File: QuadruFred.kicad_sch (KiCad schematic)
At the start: 0 parts

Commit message: Add basic leg boards and eps 32. No in depth wiring done.
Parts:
- added J1: Servo1, Connector_PinHeader_2.54mm:PinHeader_1x03_P2.54mm_Horizontal, symbol Connector:Conn_01x03_Pin
- added J10: Servo10, Connector_PinHeader_2.54mm:PinHeader_1x03_P2.54mm_Horizontal, symbol Connector:Conn_01x03_Pin
- added J11: Servo11, Connector_PinHeader_2.54mm:PinHeader_1x03_P2.54mm_Horizontal, symbol Connector:Conn_01x03_Pin
- added J12: Servo12, Connector_PinHeader_2.54mm:PinHeader_1x03_P2.54mm_Horizontal, symbol Connector:Conn_01x03_Pin
- added J2: Servo2, Connector_PinHeader_2.54mm:PinHeader_1x03_P2.54mm_Horizontal, symbol Connector:Conn_01x03_Pin
- added J3: Servo 3, Connector_PinHeader_2.54mm:PinHeader_1x03_P2.54mm_Horizontal, symbol Connector:Conn_01x03_Pin
- added J4: Servo4, Connector_PinHeader_2.54mm:PinHeader_1x03_P2.54mm_Horizontal, symbol Connector:Conn_01x03_Pin
- added J5: Servo5, Connector_PinHeader_2.54mm:PinHeader_1x03_P2.54mm_Horizontal, symbol Connector:Conn_01x03_Pin
- added J6: Servo6, Connector_PinHeader_2.54mm:PinHeader_1x03_P2.54mm_Horizontal, symbol Connector:Conn_01x03_Pin
- added J7: Servo7, Connector_PinHeader_2.54mm:PinHeader_1x03_P2.54mm_Horizontal, symbol Connector:Conn_01x03_Pin
- added J8: Servo8, Connector_PinHeader_2.54mm:PinHeader_1x03_P2.54mm_Horizontal, symbol Connector:Conn_01x03_Pin
- added J9: Servo9, Connector_PinHeader_2.54mm:PinHeader_1x03_P2.54mm_Horizontal, symbol Connector:Conn_01x03_Pin
- added U1: PCA9685PW, Package_SO:TSSOP-28_4.4x9.7mm_P0.65mm, symbol Driver_LED:PCA9685PW
- added U2: ESP32-S3-MINI-1, RF_Module:ESP32-S2-MINI-1, symbol RF_Module:ESP32-S3-MINI-1
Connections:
- new net: J7.1 (Pin_1), U1.12 (LED6)
- new net: U2.1 (GND), U2.2 (GND), U2.42 (GND), U2.43 (GND), U2.46 (GND), U2.47 (GND), U2.48 (GND), U2.49 (GND), U2.50 (GND), U2.51 (GND), U2.52 (GND), U2.53 (GND), U2.54 (GND), U2.55 (GND), U2.56 (GND), U2.57 (GND), U2.58 (GND), U2.59 (GND), U2.60 (GND), U2.61 (GND), U2.62 (GND), U2.63 (GND), U2.64 (GND), U2.65 (GND)
- new net: J8.1 (Pin_1), U1.13 (LED7)
- new net: J10.1 (Pin_1), U1.16 (LED9)
- new net: J1.1 (Pin_1), U1.6 (LED0)
- new net: J5.1 (Pin_1), U1.10 (LED4)
- new net: J6.1 (Pin_1), U1.11 (LED5)
- new net: J9.1 (Pin_1), U1.15 (LED8)
- new net: J11.1 (Pin_1), U1.17 (LED10)
- new net: J12.1 (Pin_1), U1.18 (LED11)
- new net: J2.1 (Pin_1), U1.7 (LED1)
- new net: J3.1 (Pin_1), U1.8 (LED2)
- new net: J4.1 (Pin_1), U1.9 (LED3)
- new net +5V: J1.2 (Pin_2), J10.2 (Pin_2), J11.2 (Pin_2), J12.2 (Pin_2), J2.2 (Pin_2), J3.2 (Pin_2), J4.2 (Pin_2), J5.2 (Pin_2), J6.2 (Pin_2), J7.2 (Pin_2), J8.2 (Pin_2), J9.2 (Pin_2), U1.28 (VDD)
- new net GND: J1.3 (Pin_3), J10.3 (Pin_3), J11.3 (Pin_3), J12.3 (Pin_3), J2.3 (Pin_3), J3.3 (Pin_3), J4.3 (Pin_3), J5.3 (Pin_3), J6.3 (Pin_3), J7.3 (Pin_3), J8.3 (Pin_3), J9.3 (Pin_3), U1.14 (VSS)
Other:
- note added: "Leg PWM System"
- note added: "Legs"

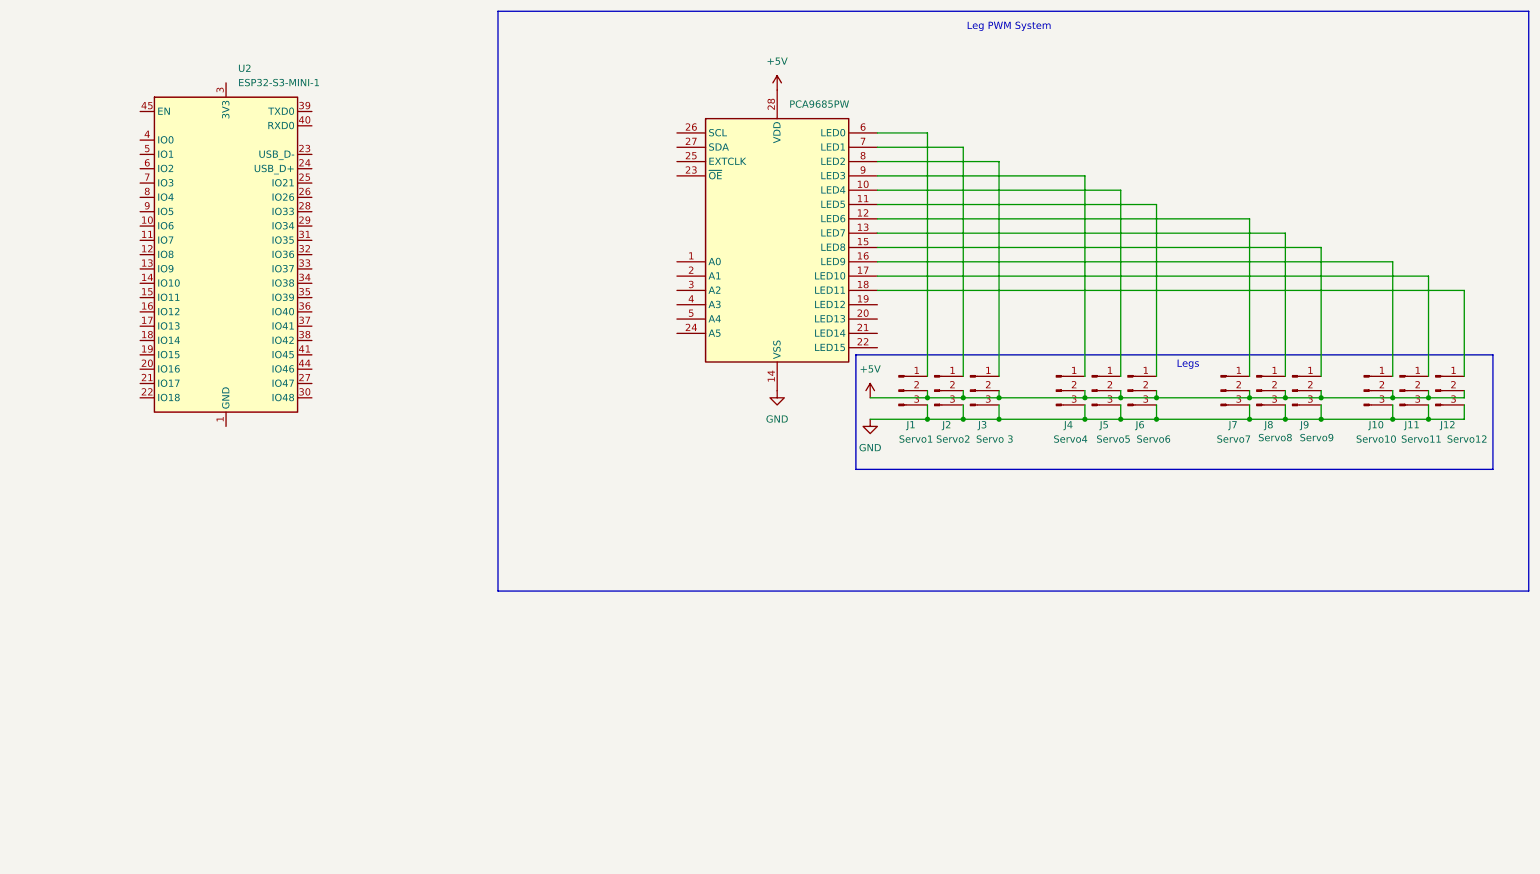
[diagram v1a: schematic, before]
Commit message: Finish USB circut and work finish ESP32 main connections
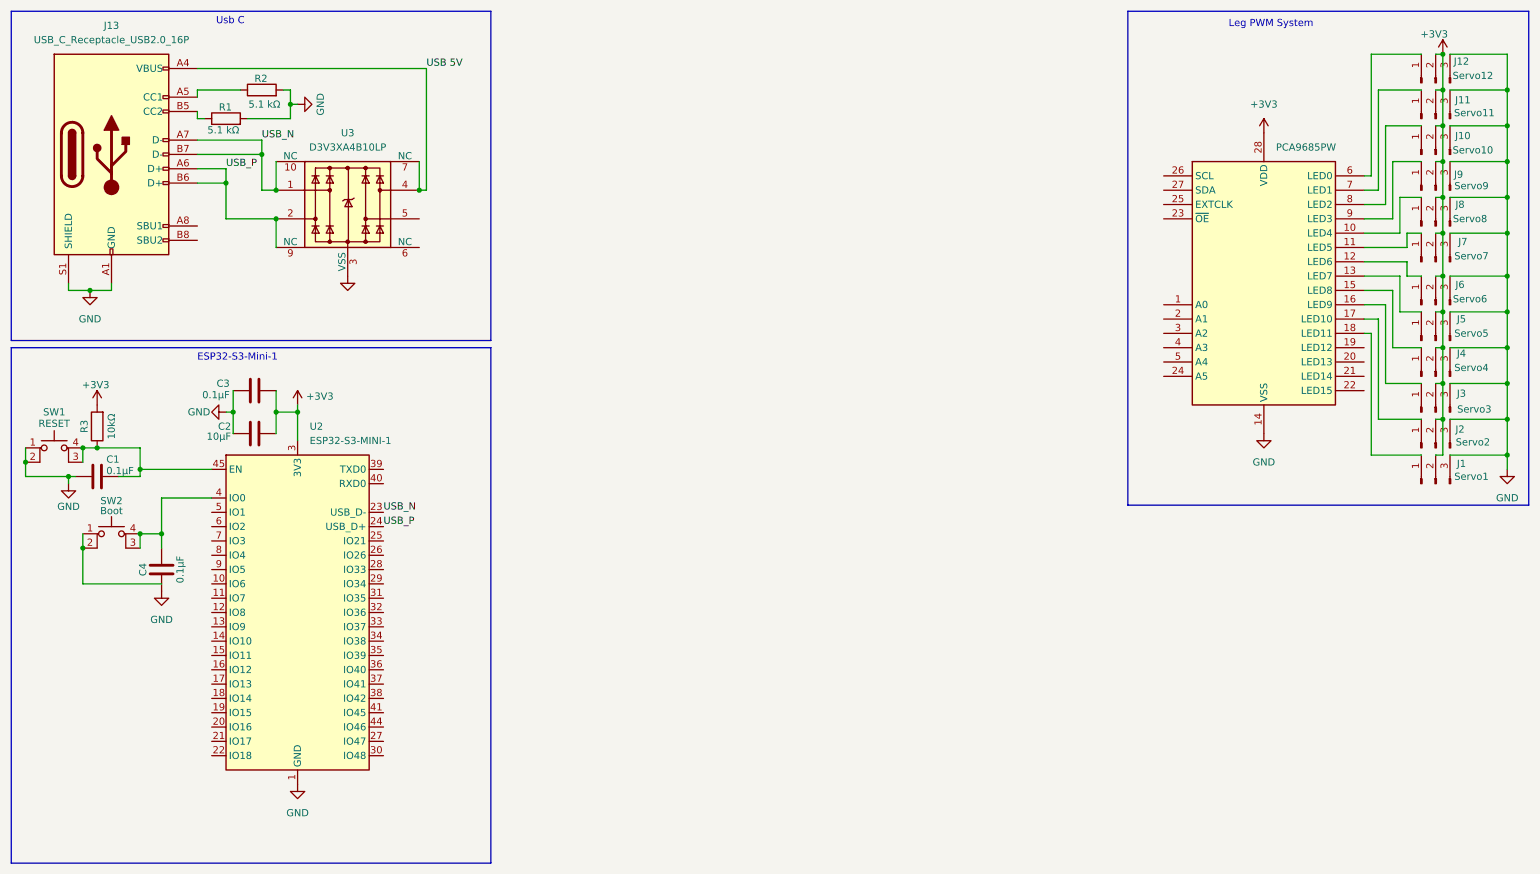
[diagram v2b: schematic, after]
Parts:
- added C1, C3, C4: 0.1µF, symbol Device:C
- added C2: 10µF, symbol Device:C
- added J13: USB_C_Receptacle_USB2.0_16P, Connector_USB:USB_C_Receptacle_GCT_USB4105-xx-A_16P_TopMnt_Horizontal, symbol Connector:USB_C_Receptacle_USB2.0_16P
- added R1, R2: 5.1 kΩ, Resistor_SMD:R_1206_3216Metric_Pad1.30x1.75mm_HandSolder, symbol Device:R
- added R3: 10kΩ, symbol Device:R
- added SW1: RESET, Button_Switch_SMD:SW_SPST_CK_KMS2xxG, symbol Switch:SW_MEC_5E
- added SW2: Boot, Button_Switch_SMD:SW_SPST_CK_KMS2xxG, symbol Switch:SW_MEC_5E
- added U3: D3V3XA4B10LP, Package_DFN_QFN:Diodes_UDFN-10_1.0x2.5mm_P0.5mm, symbol Power_Protection:D3V3XA4B10LP
- J1, J10, J11, J12, J2, J4, J5, J6, J7, J8, J9: footprint Connector_PinHeader_2.54mm:PinHeader_1x03_P2.54mm_Horizontal -> Connector_PinHeader_2.54mm:PinHeader_1x03_P2.54mm_Vertical
- J3: value Servo 3 -> Servo3; footprint Connector_PinHeader_2.54mm:PinHeader_1x03_P2.54mm_Horizontal -> Connector_PinHeader_2.54mm:PinHeader_1x03_P2.54mm_Vertical
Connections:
- net +5V is gone; now on net +3V3: J1.2 (Pin_2), J10.2 (Pin_2), J11.2 (Pin_2), J12.2 (Pin_2), J2.2 (Pin_2), J3.2 (Pin_2), J4.2 (Pin_2), J5.2 (Pin_2), J6.2 (Pin_2), J7.2 (Pin_2), J8.2 (Pin_2), J9.2 (Pin_2), U1.28 (VDD)
- net GND: now also U2.1 (GND), U2.2 (GND), U2.42 (GND), U2.43 (GND), U2.46 (GND), U2.47 (GND), U2.48 (GND), U2.49 (GND), U2.50 (GND), U2.51 (GND), U2.52 (GND), U2.53 (GND), U2.54 (GND), U2.55 (GND), U2.56 (GND), U2.57 (GND), U2.58 (GND), U2.59 (GND), U2.60 (GND), U2.61 (GND), U2.62 (GND), U2.63 (GND), U2.64 (GND), U2.65 (GND), C1.1, C2.1, C3.1, C4.1, J13.A1 (GND), J13.A12 (GND), J13.B1 (GND), J13.B12 (GND), J13.S1 (SHIELD), R1.2, R2.2, SW1.1, SW1.2, U3.3 (VSS), U3.8 (VSS)
- net at J7.1 (Pin_1): now also U1.11 (LED5); no longer U1.12 (LED6)
- net USB_N: now reaches U2.23 (USB_D-)
- net USB_N: now also J13.A7 (D-), J13.B7 (D-), U3.1, U3.10 (NC)
- net USB_P: now reaches U2.24 (USB_D+)
- net USB_P: now also J13.A6 (D+), J13.B6 (D+), U3.2, U3.9 (NC)
- net +3V3: now reaches U2.3 (3V3)
- net +3V3: now also C2.2, C3.2, R3.2
- net at U2.4 (IO0): now also C4.2, SW2.3 (K), SW2.4 (A)
- net at U2.45 (EN): now also C1.2, R3.1, SW1.3 (K), SW1.4 (A)
- net at J8.1 (Pin_1): now also U1.10 (LED4); no longer U1.13 (LED7)
- net at U1.16 (LED9): now also J3.1 (Pin_1); no longer J10.1 (Pin_1)
- net at J1.1 (Pin_1): now also U1.18 (LED11); no longer U1.6 (LED0)
- net at J5.1 (Pin_1): now also U1.13 (LED7); no longer U1.10 (LED4)
- net at J6.1 (Pin_1): now also U1.12 (LED6); no longer U1.11 (LED5)
- net at U1.15 (LED8): now also J4.1 (Pin_1); no longer J9.1 (Pin_1)
- net at J11.1 (Pin_1): now also U1.7 (LED1); no longer U1.17 (LED10)
- net at J12.1 (Pin_1): now also U1.6 (LED0); no longer U1.18 (LED11)
- net at J2.1 (Pin_1): now also U1.17 (LED10); no longer U1.7 (LED1)
- net at U1.8 (LED2): now also J10.1 (Pin_1); no longer J3.1 (Pin_1)
- net at U1.9 (LED3): now also J9.1 (Pin_1); no longer J4.1 (Pin_1)
- new net: J13.A5 (CC1), R2.1
- new net: J13.B5 (CC2), R1.1
- new net: SW2.1, SW2.2
- new net USB 5V: J13.A4 (VBUS), J13.A9 (VBUS), J13.B4 (VBUS), J13.B9 (VBUS), U3.4, U3.7 (NC)
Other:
- note added: "ESP32-S3-Mini-1"
- note added: "Usb C"
- note removed: "Legs"
- moved on the sheet: U2
